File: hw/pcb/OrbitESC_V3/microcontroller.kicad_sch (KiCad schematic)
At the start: 58 parts, among them J1 USB_C_Receptacle_USB2.0, J11 CANH, J11 CANL, J11 GND, J11 RX, J11 TX, J8 Micro_SD_Card_Det2, SW1 Reset, SW2 DFU, U1 TLE9250X, U2 AT25SF128A-SHB-T, U3 STM32F446RETx, X1 ASE-24MHz

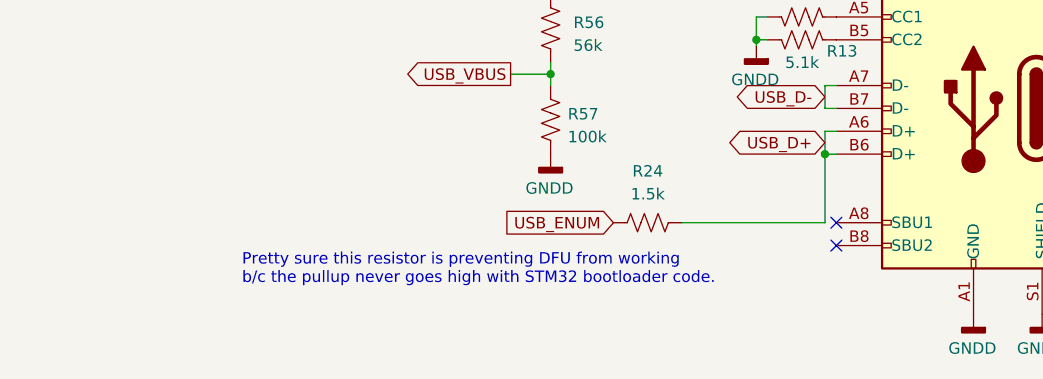
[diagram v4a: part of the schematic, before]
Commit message: Get consistent mount/unmount working
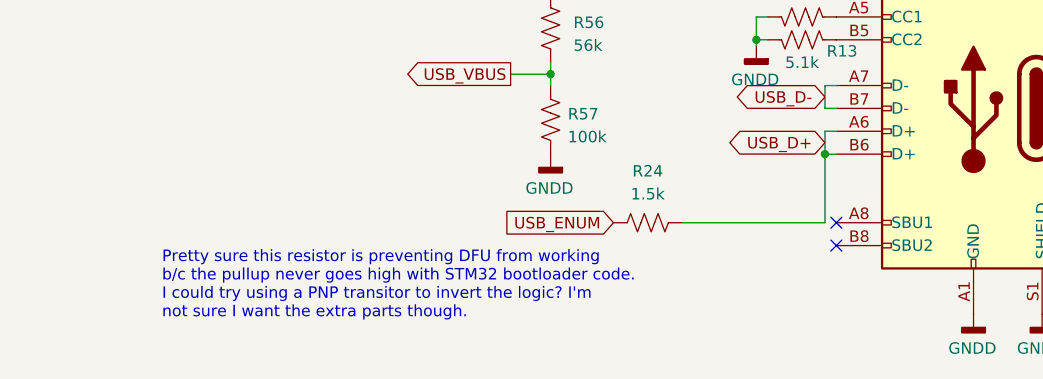
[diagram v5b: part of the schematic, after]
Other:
- note added: "Pretty sure this resistor is preventing DFU from working b/c the pullup never goes high with STM32 bootloader code. I could try using a PNP transitor to invert the logic? I'm not sure I want the extra parts though."
- note removed: "Pretty sure this resistor is preventing DFU from working b/c the pullup never goes high with STM32 bootloader code."
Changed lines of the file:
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@@
     (effects (font (size 1.27 1.27)) (justify left bottom))
   )
-  (text "Pretty sure this resistor is preventing DFU from working\nb/c the pullup never goes high with STM32 bootloader code."
-    (at 273.05 243.84 0)
+  (text "Pretty sure this resistor is preventing DFU from working\nb/c the pullup never goes high with STM32 bootloader code.\nI could try using a PNP transitor to invert the logic? I'm\nnot sure I want the extra parts though."
+    (at 264.16 247.65 0)
     (effects (font (size 1.27 1.27)) (justify left bottom))
   )

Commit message: USB is working!
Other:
- note added: "Pretty sure this resistor is preventing DFU from working b/c the pullup never goes high with STM32 bootloader code. I could try using a PNP transitor to invert the logic? I'm not sure I want the extra parts though. Update 10/28/2023: Turns out that this resistor is already embedded on the F446RE and including it under GPIO control is really messing with my software. Remove it."
- note added: "VBus sensing can be removed. When the F4 configures PA9 as an alternate function, it breaks sensing. Solution is to disable/override sensing in software and force device mode."
- note removed: "Pretty sure this resistor is preventing DFU from working b/c the pullup never goes high with STM32 bootloader code. I could try using a PNP transitor to invert the logic? I'm not sure I want the extra parts though."
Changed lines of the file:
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@@
     (effects (font (size 1.27 1.27)) (justify left bottom))
   )
-  (text "Pretty sure this resistor is preventing DFU from working\nb/c the pullup never goes high with STM32 bootloader code.\nI could try using a PNP transitor to invert the logic? I'm\nnot sure I want the extra parts though."
-    (at 264.16 247.65 0)
+  (text "Pretty sure this resistor is preventing DFU from working\nb/c the pullup never goes high with STM32 bootloader code.\nI could try using a PNP transitor to invert the logic? I'm\nnot sure I want the extra parts though.\n\nUpdate 10/28/2023: Turns out that this resistor is already\nembedded on the F446RE and including it under GPIO control\nis really messing with my software. Remove it."
+    (at 243.205 254 0)
     (effects (font (size 1.27 1.27)) (justify left bottom))
   )
+  (text "VBus sensing can be removed. When the F4 configures PA9 as\nan alternate function, it breaks sensing. Solution is to \ndisable/override sensing in software and force device mode."
+    (at 240.665 228.6 0)
+    (effects (font (size 1.27 1.27)) (justify left bottom))
+  )

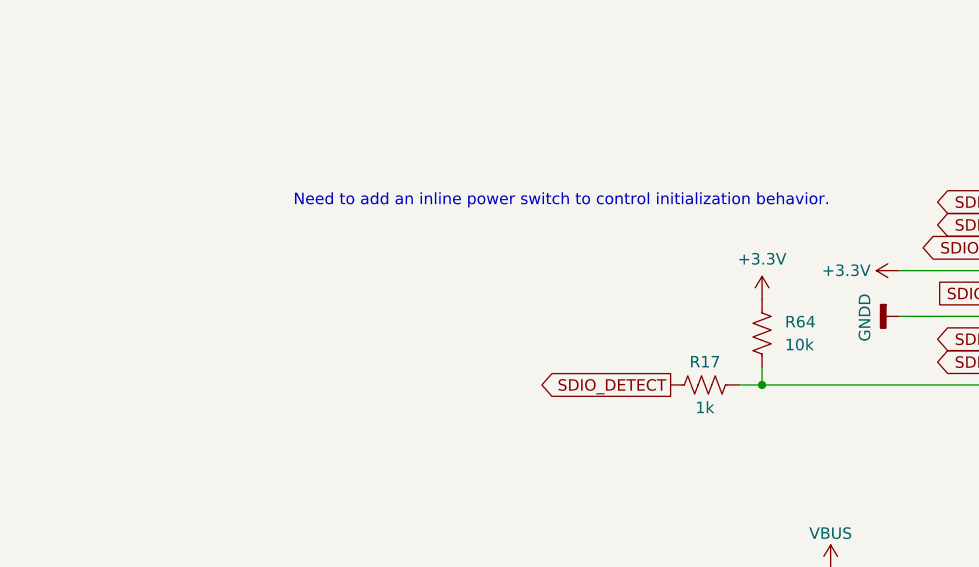
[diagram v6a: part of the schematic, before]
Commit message: Update PCB notes for v3.1
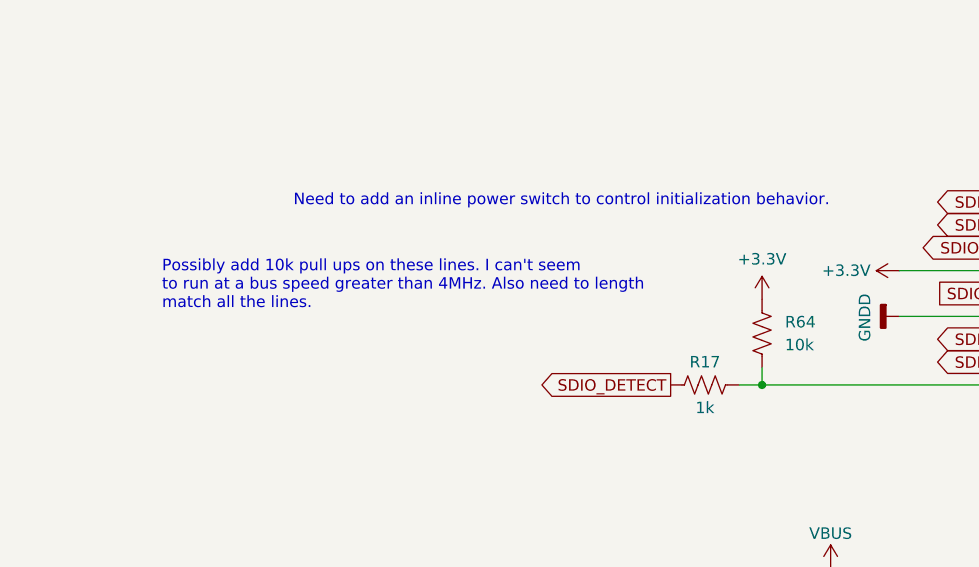
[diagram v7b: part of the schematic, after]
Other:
- note added: "Possibly add 10k pull ups on these lines. I can't seem to run at a bus speed greater than 4MHz. Also need to length match all the lines."
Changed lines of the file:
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@@
+    (effects (font (size 1.27 1.27)) (justify left bottom))
+  )
+  (text "Possibly add 10k pull ups on these lines. I can't seem\nto run at a bus speed greater than 4MHz. Also need to length\nmatch all the lines."
+    (at 233.045 182.88 0)
     (effects (font (size 1.27 1.27)) (justify left bottom))
   )

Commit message: Sync some ideas from messing around
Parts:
- renumbered C29 to C3, C13 to C37, C29 to C46, C36 to C47, C13 to C6, C29 to C8, J11 to J13, J11 to J2, J11 to J6, J11 to J7, J11 to J9, R23 to R54, R17 to R65, R24 to R66, TP1 to TP2
